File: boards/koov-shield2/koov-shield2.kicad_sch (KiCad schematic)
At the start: 26 parts, among them J1 Power, J2 Digital/PWM, J3 Analog, J4 Digital/PWM, SW1 SW_DPDT, U1 DRV8835DSSR

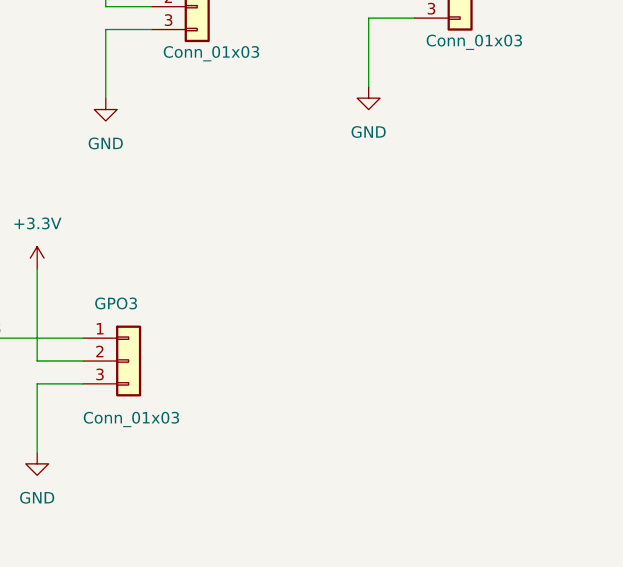
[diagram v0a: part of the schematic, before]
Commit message: Wiring UARTs to the unused connector.
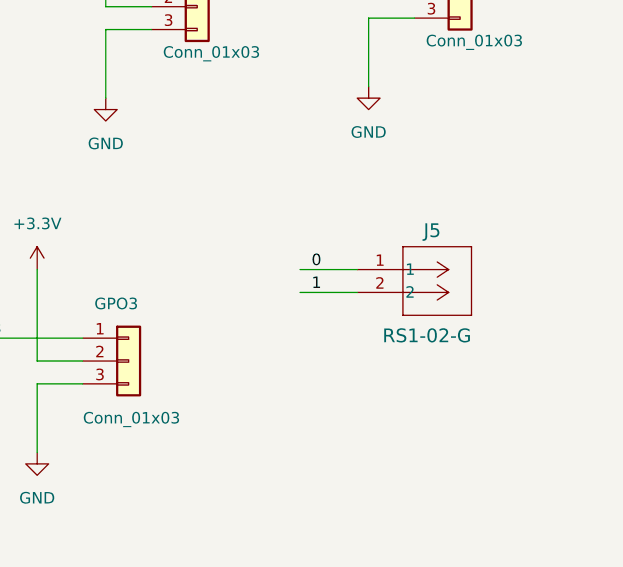
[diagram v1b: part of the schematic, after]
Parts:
- added J5: RS1-02-G, CONN_RS1-02-G_ADM, symbol 2025-03-12_10-05-33:RS1-02-G
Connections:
- net 0: now also J5.1
- net 1: now also J5.2
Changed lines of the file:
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@@
 	(wire
 		(pts
+			(xy 243.84 64.77) (xy 250.19 64.77)
+		)
+		(stroke
+			(width 0)
+			(type default)
+		)
+	)
+	(wire
+		(pts
 			(xy 27.94 137.16) (xy 27.94 147.32)
 		)
@@
 	(wire
 		(pts
+			(xy 243.84 62.23) (xy 250.19 62.23)
+		)
+		(stroke
+			(width 0)
+			(type default)
+		)
+	)
+	(wire
+		(pts
 			(xy 53.34 147.32) (xy 58.42 147.32)
 		)
@@
 		)
 	)
+	(label "1"
+		(at 245.11 64.77 0)
+		(fields_autoplaced yes)
+		(effects
+			(font
+				(size 1.27 1.27)
+			)
+			(justify left bottom)
+		)
+	)
 	(label "2"
 		(at 139.7 69.85 0)
@@
 		)
 	)
+	(label "0"
+		(at 245.11 62.23 0)
+		(fields_autoplaced yes)
+		(effects
+			(font
+				(size 1.27 1.27)
+			)
+			(justify left bottom)
+		)
+	)
 	(label "*6"
 		(at 195.58 139.7 0)
@@
 					(unit 1)
 				)
+			)
+		)
+	)
+	(symbol
+		(lib_id "2025-03-12_10-05-33:RS1-02-G")
+		(at 250.19 62.23 0)
+		(unit 1)
+		(exclude_from_sim no)
+		(in_bom yes)
+		(on_board yes)
+		(dnp no)
+		(property "Reference" "J5"
+			(at 257.556 57.912 0)
+			(effects
+				(font
+					(size 1.524 1.524)
+				)
+				(justify left)
+			)
+		)
+		(property "Value" "RS1-02-G"
+			(at 252.984 69.596 0)
+			(effects
+				(font
+					(size 1.524 1.524)
+				)
+				(justify left)
+			)
+		)
+		(property "Footprint" "CONN_RS1-02-G_ADM"
+			(at 250.19 62.23 0)
+			(effects
+				(font
+					(size 1.27 1.27)
+					(italic yes)
+				)
+				(hide yes)
+			)
+		)
+		(property "Datasheet" "RS1-02-G"
+			(at 250.19 62.23 0)
+			(effects
+				(font
+					(size 1.27 1.27)
+					(italic yes)
+				)
+				(hide yes)
+			)
+		)
+		(property "Description" ""
+			(at 250.19 62.23 0)
+			(effects
+				(font
+					(size 1.27 1.27)
+				)
+				(hide yes)
+			)
+		)
+		(pin "2"
+		)
+		(pin "1"
+		)
+		(instances
+			(project ""
+				(path "/e63e39d7-6ac0-4ffd-8aa3-1841a4541b55"
+					(reference "J5")
+					(unit 1)
+				)

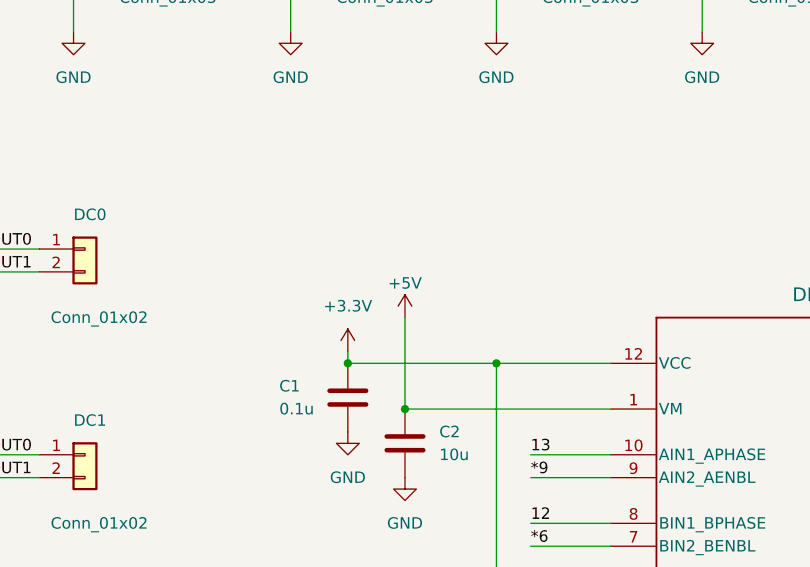
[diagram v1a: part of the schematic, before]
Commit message: fix swirch miss.
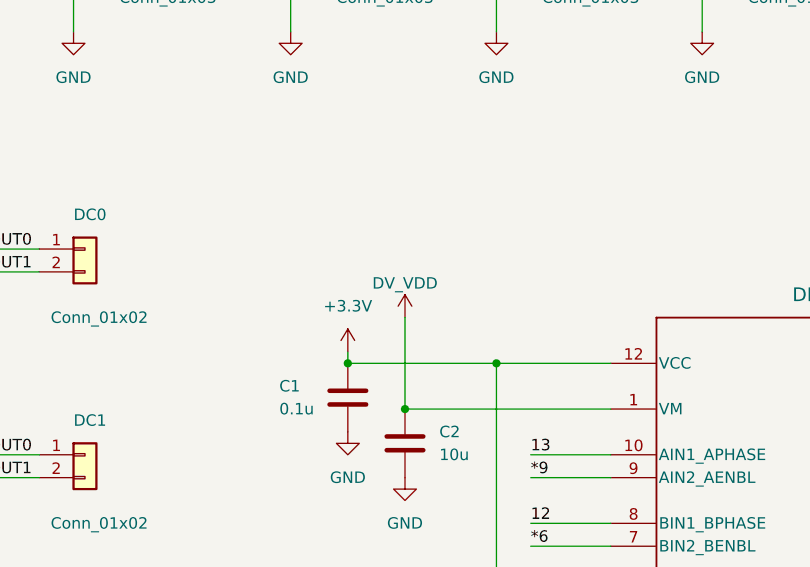
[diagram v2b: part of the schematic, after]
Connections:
- net +5V: no longer C2.1, U1.1 (VM)
- net DV_VDD: now also C2.1, U1.1 (VM)
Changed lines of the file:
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@@
 			)
 		)
-		(property "Value" "+5V"
+		(property "Value" "DV_VDD"
 			(at 181.61 110.49 0)
 			(effects
